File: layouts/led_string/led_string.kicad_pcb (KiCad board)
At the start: 2 copper layers, 5 parts

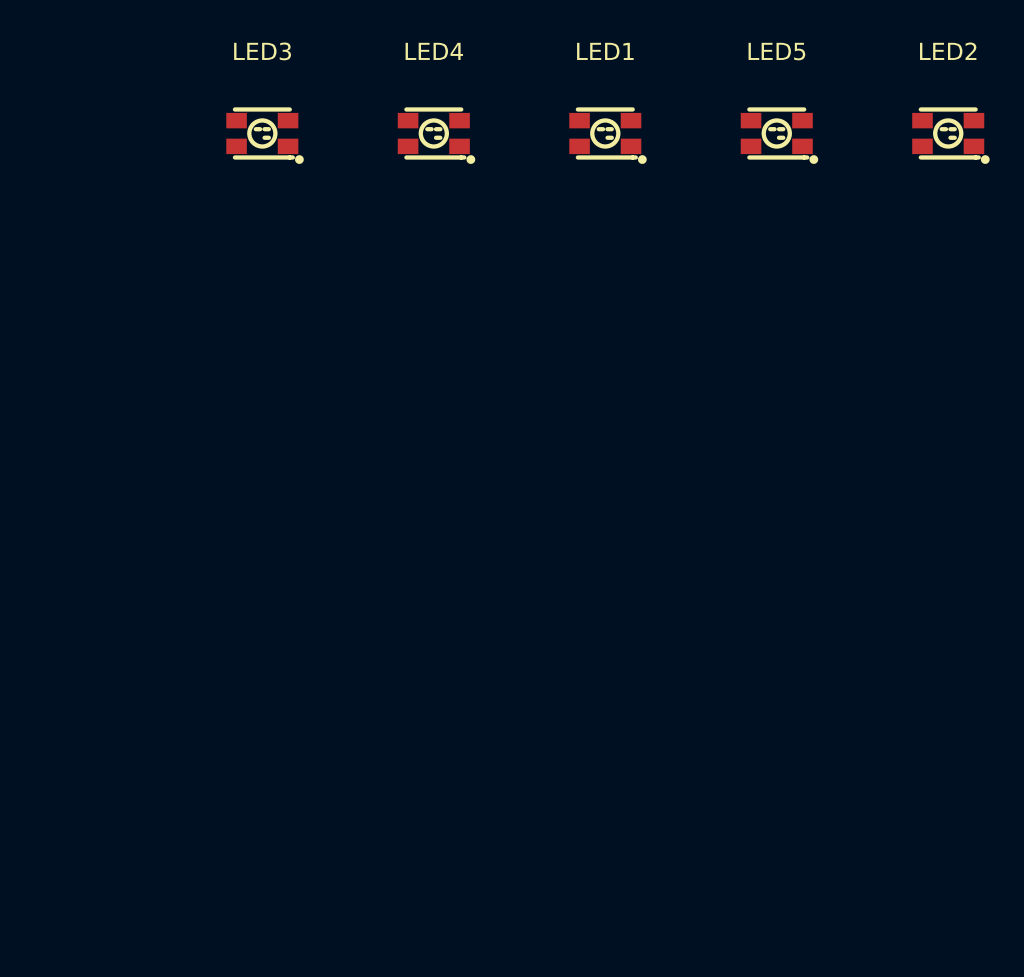
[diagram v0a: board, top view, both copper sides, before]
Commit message: Add MCU as build target
use this ato branch to fix build:
https://github.com/atopile/atopile/pull/979
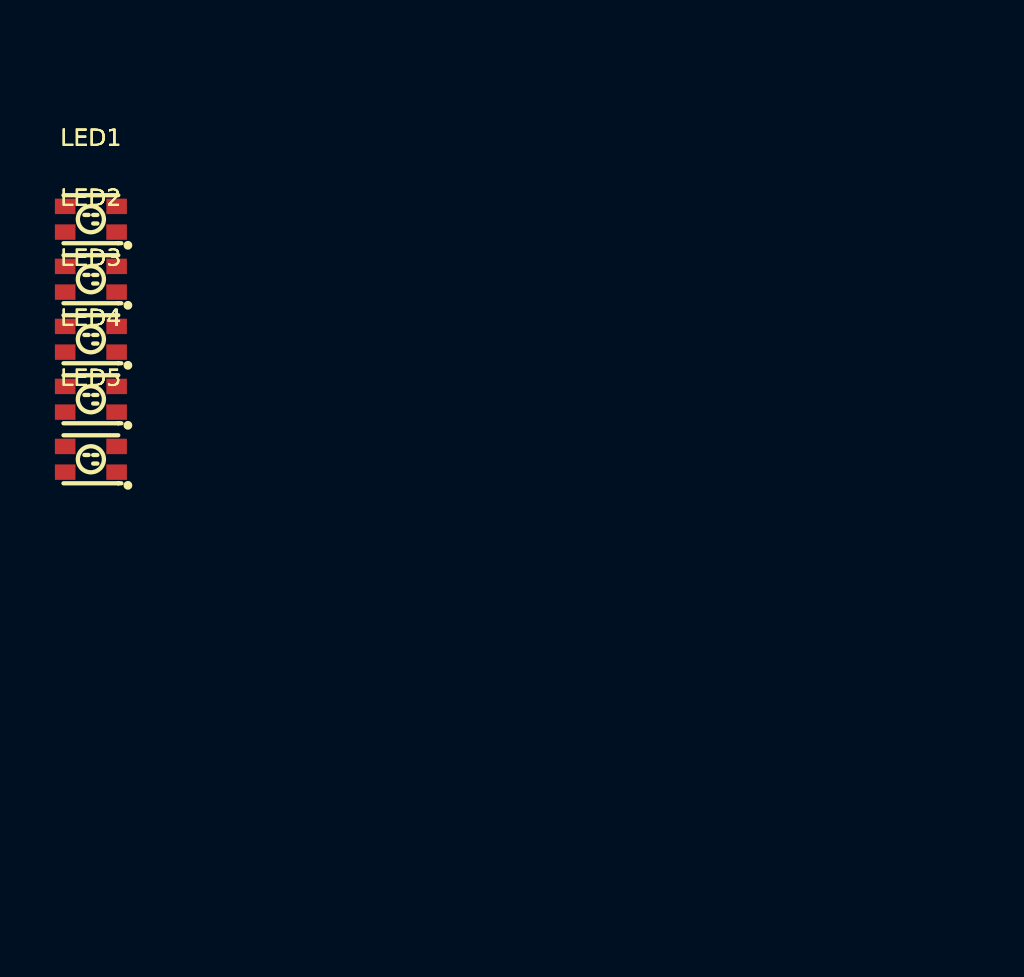
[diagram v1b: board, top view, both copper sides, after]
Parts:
- moved LED2 50.7 mm to (0.00, 3.50)
- moved LED5 44.3 mm to (0.00, 14.0)
- moved LED1 30.4 mm to (0.00, 0.00)
- moved LED4 25.3 mm to (0.00, 10.5)
- moved LED3 15.6 mm to (0.00, 7.00)
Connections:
- LED1 pad 2: line-3 -> line-4
- LED1 pad 4: line-4 -> line-1
- LED2 pad 2: line-4 -> line-1
- LED2 pad 4: line-1 -> line-3
- LED3 pad 2: line-1 -> line-3

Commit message: Migrate layout partially
omit routing and zones amongst others
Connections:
- LED1 pad 4: line-1 -> line
- LED2 pad 2: line-1 -> line
- LED2 pad 4: line-3 -> line-1
- LED3 pad 2: line-3 -> line-1
- LED3 pad 4: line -> line-3
- LED4 pad 2: line -> line-3
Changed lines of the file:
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@@
     (net 0 "")
     (net 1 "line-2")
-    (net 2 "line-1")
+    (net 2 "line")
     (net 3 "hv")
     (net 4 "line-4")
-    (net 5 "line-3")
+    (net 5 "line-1")
     (net 6 "leds[4]-line")
-    (net 7 "line")
+    (net 7 "line-3")
     (net 8 "gnd")
     (footprint "atopile:LED-SMD_4P-L3.5-W2.8-BR-1-15b4e8"
@@
             (layers "F.Cu" "F.Paste" "F.Mask")
             (remove_unused_layers no)
-            (net 2 "line-1")))
+            (net 2 "line")))
     (footprint "atopile:LED-SMD_4P-L3.5-W2.8-BR-1-15b4e8"
         (layer "F.Cu")
@@
             (layers "F.Cu" "F.Paste" "F.Mask")
             (remove_unused_layers no)
-            (net 2 "line-1"))
+            (net 2 "line"))
         (pad "3" smd rect
             (at -1.5 -0.75 180)
@@
             (layers "F.Cu" "F.Paste" "F.Mask")
             (remove_unused_layers no)
-            (net 5 "line-3")))
+            (net 5 "line-1")))
     (footprint "atopile:LED-SMD_4P-L3.5-W2.8-BR-1-15b4e8"
         (layer "F.Cu")
@@
             (layers "F.Cu" "F.Paste" "F.Mask")
             (remove_unused_layers no)
-            (net 5 "line-3"))
+            (net 5 "line-1"))
         (pad "3" smd rect
             (at -1.5 -0.75 180)
@@
             (layers "F.Cu" "F.Paste" "F.Mask")
             (remove_unused_layers no)
-            (net 7 "line")))
+            (net 7 "line-3")))
     (footprint "atopile:LED-SMD_4P-L3.5-W2.8-BR-1-15b4e8"
         (layer "F.Cu")
@@
             (layers "F.Cu" "F.Paste" "F.Mask")
             (remove_unused_layers no)
-            (net 7 "line"))
+            (net 7 "line-3"))
         (pad "3" smd rect
             (at -1.5 -0.75 180)

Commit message: Regenerate layouts
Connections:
- LED1 pad 2: line-4 -> line-1
- LED1 pad 4: line -> line-4
- LED2 pad 2: line -> line-4
- LED2 pad 4: line-1 -> line
- LED3 pad 2: line-1 -> line
- LED3 pad 4: line-3 -> line-2
- LED4 pad 2: line-3 -> line-2
- LED4 pad 4: line-2 -> line-3
- LED5 pad 2: line-2 -> line-3

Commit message: Update layouts
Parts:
- added U1: , atopile:VSON8_L2.0-W2.3-P0.50-LS3.1-BL-9e6526, F.Cu at (4.70, 0.00)
- moved LED5 15.0 mm to (0.00, 29.0)
- moved LED4 11.2 mm to (0.00, 21.8)
- moved LED3 7.50 mm to (0.00, 14.5)
- moved LED2 3.75 mm to (0.00, 7.25)
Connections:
- net hv renamed hv-1
- LED1 pad 2: line-1 -> line-3
- LED1 pad 4: line-4 -> line
- LED2 pad 2: line-4 -> line
- LED2 pad 4: line -> line-5
- LED3 pad 2: line -> line-5
- LED4 pad 4: line-3 -> line-4
- LED5 pad 2: line-3 -> line-4
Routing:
- net line-5: track 0.00 -> 6.99 mm
- net line-4: track 0.00 -> 6.99 mm
- net line-2: track 0.00 -> 6.99 mm
- net line: track 0.00 -> 6.99 mm
- net line-3: track 0.00 -> 2.77 mm

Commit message: Update layout
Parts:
- added C1: 100nF ±10% 16V X7R, atopile:C0402-b3ef17, B.Cu at (1.50, 3.00)
- added C2: 100nF ±10% 16V X7R, atopile:C0402-b3ef17, B.Cu at (1.50, 9.00)
- added C3: 100nF ±10% 16V X7R, atopile:C0402-b3ef17, B.Cu at (1.50, 15.2)
- added C4: 100nF ±10% 16V X7R, atopile:C0402-b3ef17, B.Cu at (1.50, 21.2)
- added C5: 100nF ±10% 16V X7R, atopile:C0402-b3ef17, B.Cu at (1.50, 27.2)
- LED1, LED2, LED3, LED4, LED5: moved to B.Cu
- moved U1 20.0 mm to (-1.50, 19.0)
- moved LED5 4.60 mm to (0.00, 24.4), turned to 180 degrees
- moved LED4 3.45 mm to (0.00, 18.3), turned to 180 degrees
- moved LED3 2.30 mm to (0.00, 12.2), turned to 180 degrees
- moved LED2 1.15 mm to (0.00, 6.10), turned to 180 degrees
- turned LED1 to 180 degrees
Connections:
- LED1 pad 2: line-3 -> line-5
- LED2 pad 4: line-5 -> line-4
- LED3 pad 2: line-5 -> line-4
- LED4 pad 4: line-4 -> line-1
- LED5 pad 2: line-4 -> line-1
- U1 pad 1: runtime_anon[0]-line-1 -> runtime_anon[0]-line
- U1 pad 4: runtime_anon[0]-line -> runtime_anon[0]-line-1
- U1 pad 5: line-1 -> line-3
- U1 pad 8: line-3 -> line-5
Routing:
- net hv-1: track 0.00 -> 38.0 mm
- net line-1: track 0.00 -> 9.81 mm
- net line-5: track 6.99 -> 0.00 mm
- net line-2: track 6.99 -> 9.81 mm
- net line-4: track 6.99 -> 9.81 mm
- net line: track 6.99 -> 9.81 mm
- net line-3: track 2.77 -> 0.00 mm

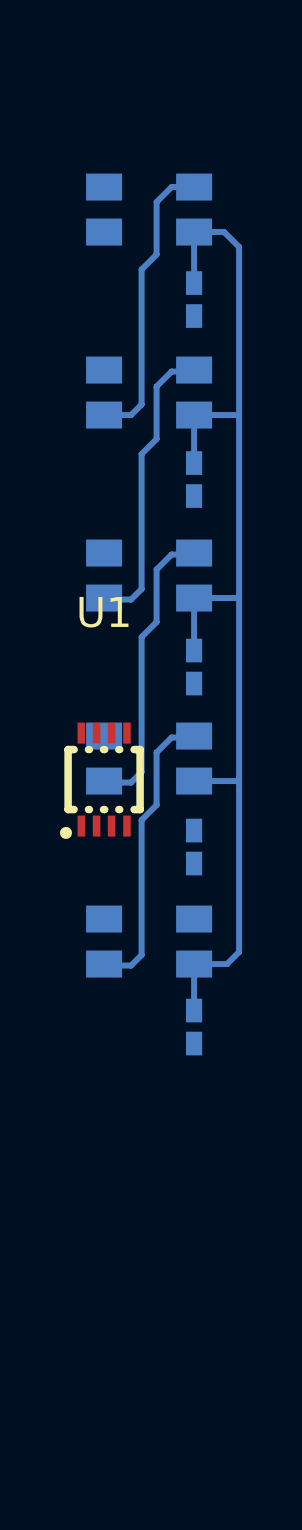
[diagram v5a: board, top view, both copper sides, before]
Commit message: Layouts: led string: fix led string layout, increase leds to 9
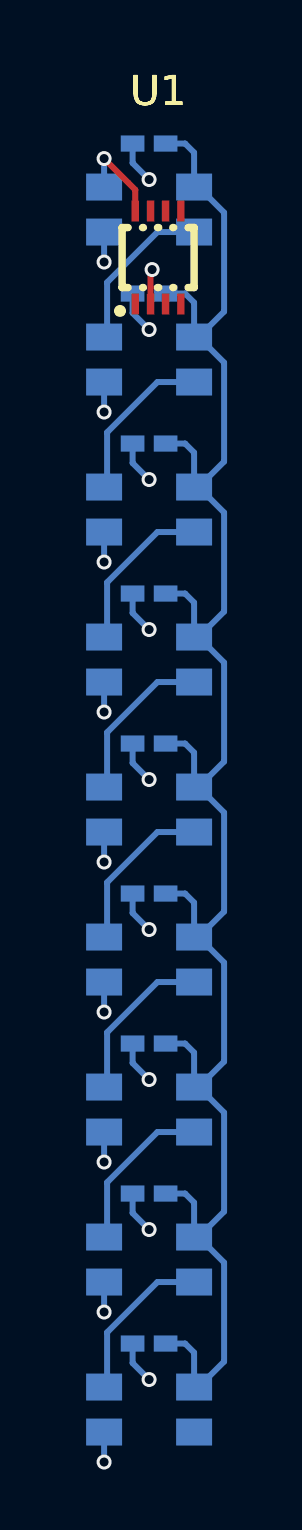
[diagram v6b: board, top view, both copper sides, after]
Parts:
- added C6: 100nF ±10% 16V X7R, atopile:C0402-b3ef17, B.Cu at (0.00, 22.8)
- added C7: 100nF ±10% 16V X7R, atopile:C0402-b3ef17, B.Cu at (0.00, 27.8)
- added C8: 100nF ±10% 16V X7R, atopile:C0402-b3ef17, B.Cu at (0.00, 32.8)
- added C9: 100nF ±10% 16V X7R, atopile:C0402-b3ef17, B.Cu at (0.00, 37.8)
- added LED6: , atopile:LED-SMD_4P-L3.5-W2.8-BR-1-15b4e8, B.Cu at (0.00, 25.0)
- added LED7: , atopile:LED-SMD_4P-L3.5-W2.8-BR-1-15b4e8, B.Cu at (0.00, 30.0)
- added LED8: , atopile:LED-SMD_4P-L3.5-W2.8-BR-1-15b4e8, B.Cu at (0.00, 35.0)
- added LED9: , atopile:LED-SMD_4P-L3.5-W2.8-BR-1-15b4e8, B.Cu at (0.00, 40.0)
- moved U1 17.5 mm to (0.30, 1.60)
- moved C5 9.57 mm to (0.00, 17.8), turned to 180 degrees
- moved C4 8.58 mm to (0.00, 12.8), turned to 180 degrees
- moved C3 7.60 mm to (0.00, 7.80), turned to 180 degrees
- moved C2 6.38 mm to (0.00, 2.80), turned to 180 degrees
- moved C1 5.41 mm to (0.00, -2.20), turned to 180 degrees
- moved LED5 4.40 mm to (0.00, 20.0)
- moved LED4 3.30 mm to (0.00, 15.0)
- moved LED3 2.20 mm to (0.00, 10.0)
- moved LED2 1.10 mm to (0.00, 5.00)
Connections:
- LED1 pad 2: line-5 -> line-7
- LED1 pad 4: line -> line-9
- LED2 pad 2: line -> line-9
- LED2 pad 4: line-4 -> line
- LED3 pad 2: line-4 -> line
- LED3 pad 4: line-2 -> line-3
- LED4 pad 2: line-2 -> line-3
- LED4 pad 4: line-1 -> line-2
- LED5 pad 2: line-1 -> line-2
- LED5 pad 4: leds[4]-line -> line-5
- U1 pad 1: runtime_anon[0]-line -> runtime_anon[0]-line-1
- U1 pad 4: runtime_anon[0]-line-1 -> runtime_anon[0]-line
- U1 pad 5: line-3 -> line-1
- U1 pad 8: line-5 -> line-7
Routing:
- net hv-1: track 38.0 -> 67.9 mm
- net gnd: track 0.00 -> 23.0 mm, vias 0 -> 19
- net line-1: track 9.81 -> 0.00 mm
- net line-9: track 0.00 -> 5.42 mm
- net line-5: track 0.00 -> 5.42 mm
- net line-3: track 0.00 -> 5.42 mm
- net line-8: track 0.00 -> 5.42 mm
- net line-6: track 0.00 -> 5.42 mm
- net line-2: track 9.81 -> 5.42 mm
- net line-4: track 9.81 -> 5.42 mm
- net line: track 9.81 -> 5.42 mm
- net line-7: track 0.00 -> 3.13 mm, vias 0 -> 1

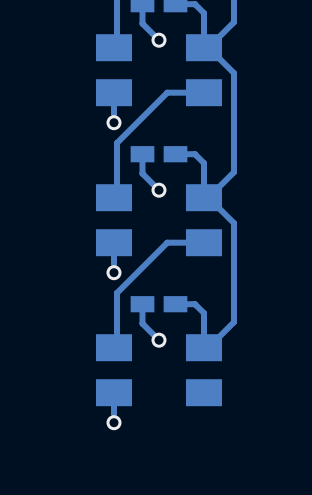
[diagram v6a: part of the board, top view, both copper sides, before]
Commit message: Layouts: place light sensor between LEDs, add rule areas
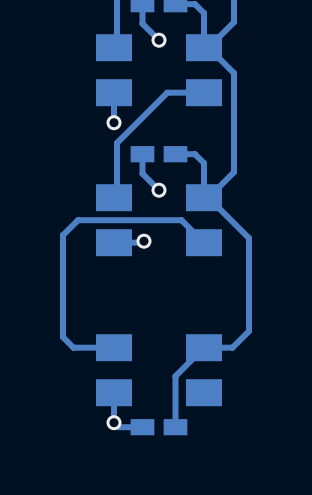
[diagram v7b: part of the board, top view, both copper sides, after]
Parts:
- moved C9 4.10 mm to (0.00, 41.9)
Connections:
- C1 pad 1: hv-1 -> hv
- C2 pad 1: hv-1 -> hv
- C3 pad 1: hv-1 -> hv
- C4 pad 1: hv-1 -> hv
- C5 pad 1: hv-1 -> hv
- C6 pad 1: hv-1 -> hv
- C7 pad 1: hv-1 -> hv
- C8 pad 1: hv-1 -> hv
- C9 pad 1: hv-1 -> hv
- LED1 pad 2: line-7 -> line-1
- LED1 pad 3: hv-1 -> hv
- LED1 pad 4: line-9 -> line-4
- LED2 pad 2: line-9 -> line-4
- LED2 pad 3: hv-1 -> hv
- LED2 pad 4: line -> line-7
- LED3 pad 2: line -> line-7
- LED3 pad 3: hv-1 -> hv
- LED3 pad 4: line-3 -> line
- LED4 pad 2: line-3 -> line
- LED4 pad 3: hv-1 -> hv
- LED4 pad 4: line-2 -> line-9
- LED5 pad 2: line-2 -> line-9
- LED5 pad 3: hv-1 -> hv
- LED5 pad 4: line-5 -> line-8
- LED6 pad 2: line-5 -> line-8
- LED6 pad 3: hv-1 -> hv
- LED6 pad 4: line-4 -> line-5
- LED7 pad 2: line-4 -> line-5
- LED7 pad 3: hv-1 -> hv
- LED7 pad 4: line-6 -> line-3
- LED8 pad 2: line-6 -> line-3
- LED8 pad 3: hv-1 -> hv
- LED8 pad 4: line-8 -> line-6
- LED9 pad 2: line-8 -> line-6
- LED9 pad 3: hv-1 -> hv
- U1 pad 3: hv -> hv-1
- U1 pad 5: line-1 -> line-2
- U1 pad 6: hv -> hv-1
- U1 pad 7: hv-1 -> hv
- U1 pad 8: line-7 -> line-1
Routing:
- net hv: track 0.00 -> 69.6 mm
- net hv-1: track 67.9 -> 0.00 mm
- net line-2: track 5.42 -> 0.00 mm
- net line-6: track 5.42 -> 10.5 mm
- net line-1: track 0.00 -> 3.13 mm, vias 0 -> 1
- net line-7: track 3.13 -> 5.42 mm, vias 1 -> 0
- net gnd: track 23.0 -> 22.6 mm, vias 19 -> 18

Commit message: do some layouts
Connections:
- LED1 pad 2: line-1 -> line-9
- LED1 pad 4: line-4 -> line-7
- LED2 pad 2: line-4 -> line-7
- LED2 pad 4: line-7 -> line
- LED3 pad 2: line-7 -> line
- LED3 pad 4: line -> line-3
- LED4 pad 2: line -> line-3
- LED4 pad 4: line-9 -> line-2
- LED5 pad 2: line-9 -> line-2
- LED5 pad 4: line-8 -> line-6
- LED6 pad 2: line-8 -> line-6
- LED6 pad 4: line-5 -> line-8
- LED7 pad 2: line-5 -> line-8
- LED7 pad 4: line-3 -> line-4
- LED8 pad 2: line-3 -> line-4
- LED8 pad 4: line-6 -> line-5
- LED9 pad 2: line-6 -> line-5
- U1 pad 5: line-2 -> line-1
- U1 pad 8: line-1 -> line-9
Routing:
- net line-2: track 0.00 -> 5.42 mm
- net line-6: track 10.5 -> 5.42 mm
- net line-5: track 5.42 -> 10.5 mm
- net line-1: track 3.13 -> 0.00 mm, vias 1 -> 0
- net line-9: track 5.42 -> 3.13 mm, vias 0 -> 1
